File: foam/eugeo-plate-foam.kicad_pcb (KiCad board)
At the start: 2 copper layers, 113.5 x 75.4 mm, 0 parts

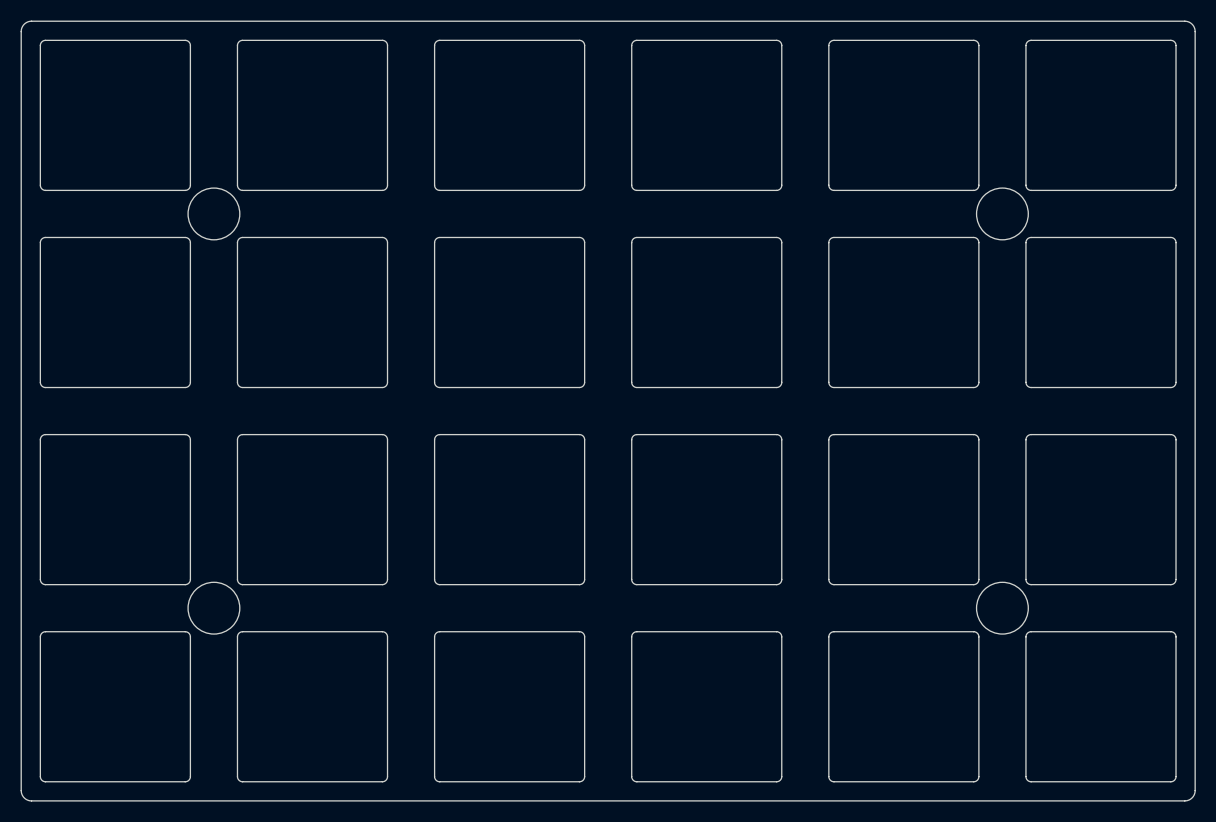
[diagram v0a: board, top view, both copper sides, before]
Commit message: Add Yushakobo laser-cut SVGs and pre-order checks
- lasercut/yushakobo: centre cover (clear acrylic 2 mm), switch plates
  (POM 1.5 mm) and plate/case foams (PORON 3 mm) laid out on Yushakobo's
  official Inkscape templates, with export and rule-check scripts
- plate foam: 3 mm PORON, standoff holes 4.4 mm to keep a 1 mm web
- scripts/preorder_check.py: revision diff, placement, hardware vs exposed
  copper, via tenting, JLCPCB minimums, Gerber freshness, drill/CPL/plate
  alignment, laser-cut SVG rules and functional checks (22/22 pass)

Co-Authored-By: Claude Opus 5.5 <noreply@anthropic.com>
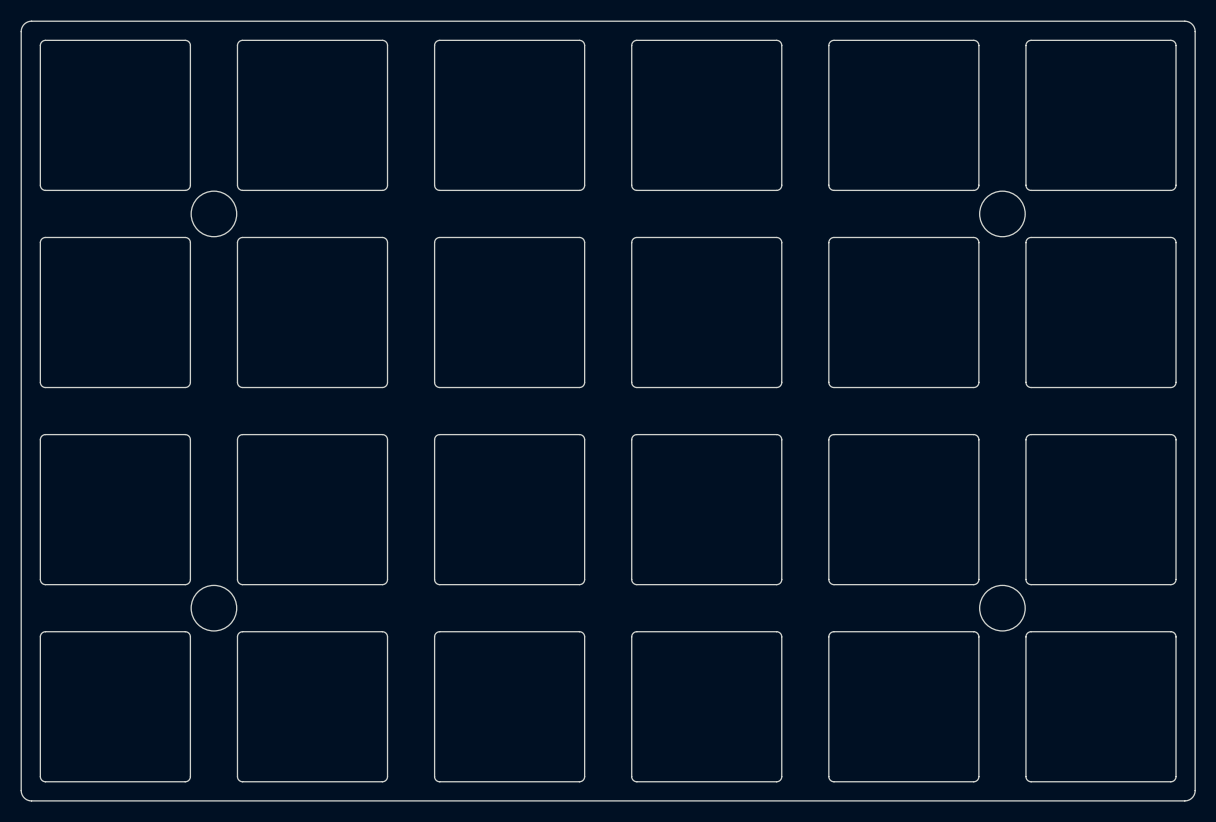
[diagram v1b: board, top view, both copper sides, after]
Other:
- outline, holes or cut-outs redrawn
- board text added: "eugeo plate foam - cut 2, 3 mm PORON"
- board text removed: "eugeo plate foam - cut 2 (flip one), 3.5 mm PORON / PE"
